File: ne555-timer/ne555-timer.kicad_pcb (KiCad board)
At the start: 2 copper layers, 29 x 21 mm, 10 parts, among them J1 Conn_01x02_Pin, U1 NE555D

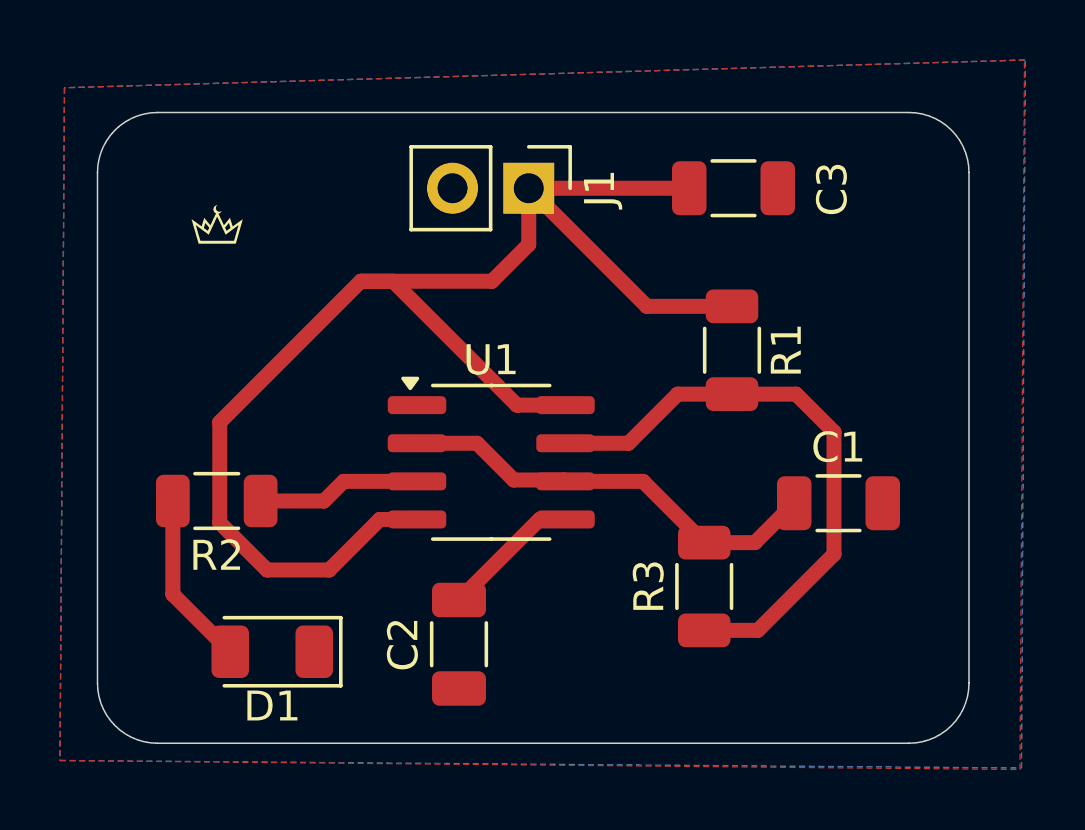
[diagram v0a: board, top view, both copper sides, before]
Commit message: zar devresi şematiği eklendi ve pcb listesi yenilendi
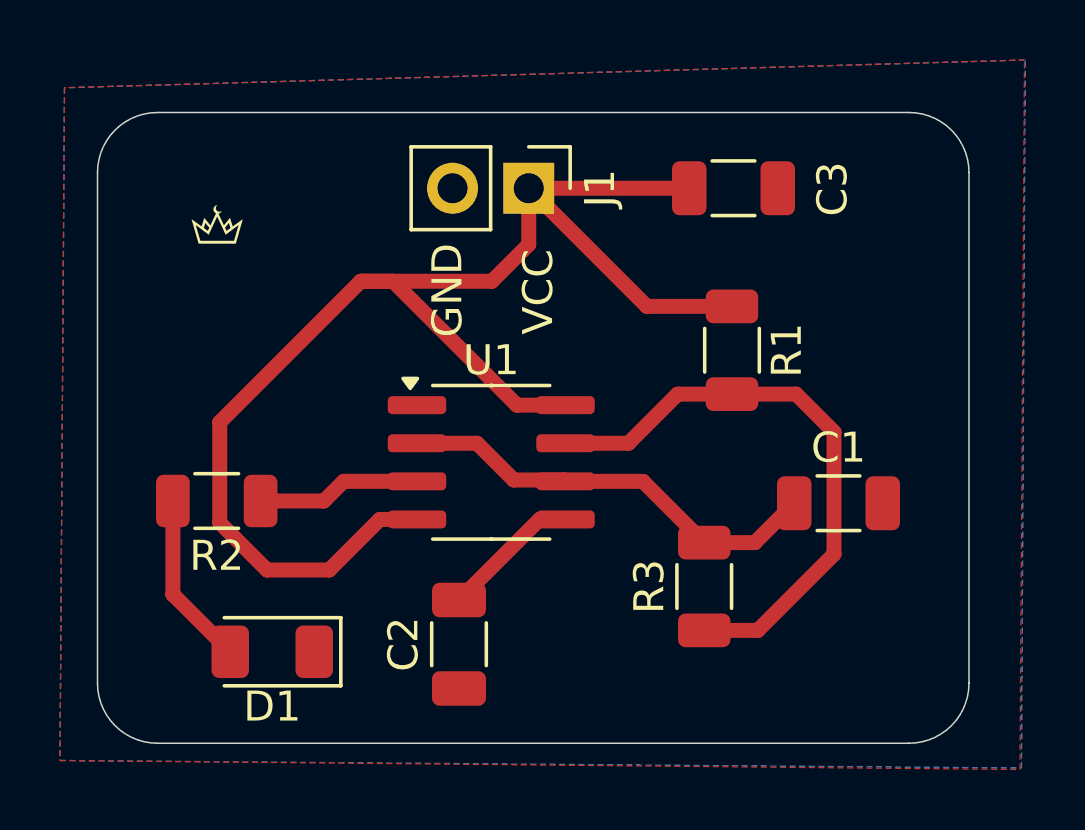
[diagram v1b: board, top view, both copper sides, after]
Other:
- board text added: "GND"
- board text added: "VCC"
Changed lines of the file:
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@@
 		(layer "Edge.Cuts")
+	)
+	(gr_text "VCC\n"
+		(at 131.675 91.754762 90)
+		(layer "F.SilkS")
+		(effects
+			(font
+				(size 1 1)
+				(thickness 0.1)
+			)
+			(justify left bottom)
+		)
+	)
+	(gr_text "GND"
+		(at 128.65 91.85 90)
+		(layer "F.SilkS")
+		(effects
+			(font
+				(size 1 1)
+				(thickness 0.1)
+			)
+			(justify left bottom)
+		)
 	)
 	(segment
